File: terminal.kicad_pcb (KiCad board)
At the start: 2 copper layers, 135 x 75 mm, 41 parts, among them J1 L77HDE15SD1CH4F-ND, J2 Mini-DIN-6, J3 UART Connector, J4 DEBUG UART HEADER, J5 Power, Q1 BSS138, Q2 BSS138, SW1 CT2088-ND, U1 CYC1000, U2 MAX3232

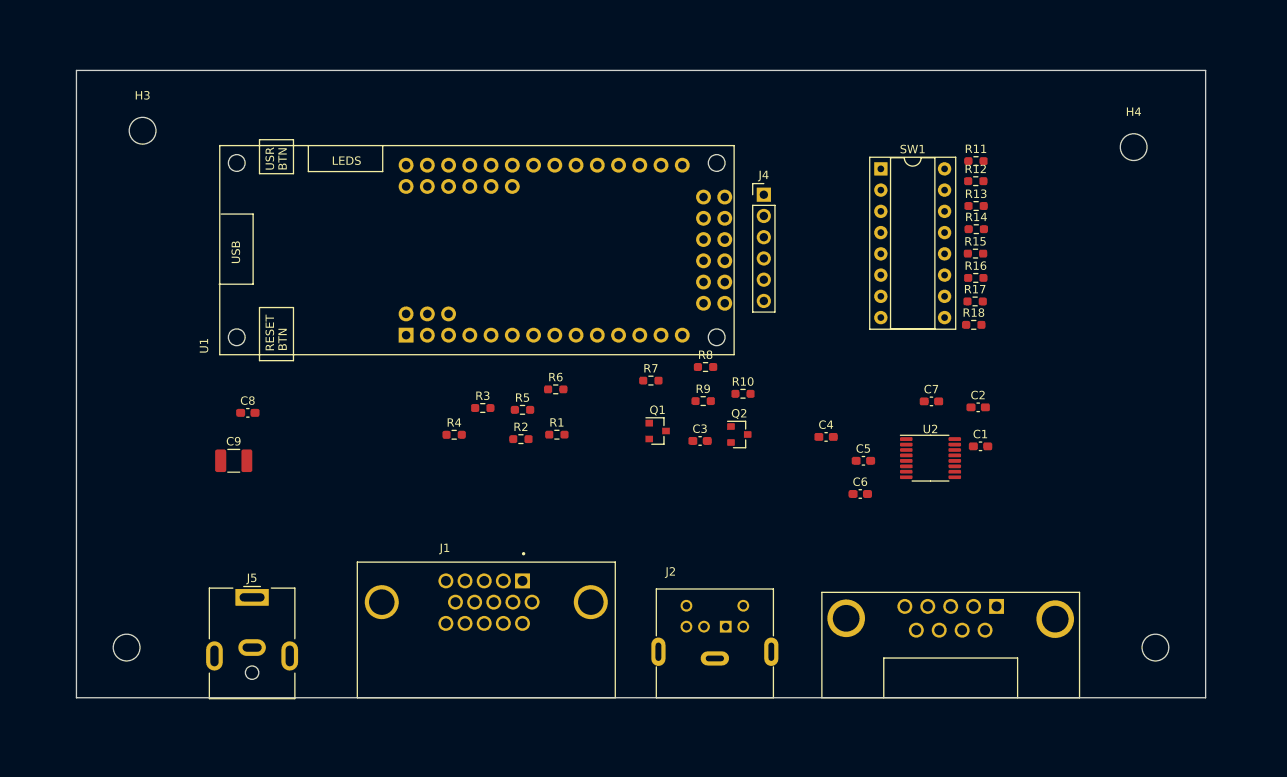
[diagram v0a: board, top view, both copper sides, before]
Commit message: Wiring connectors
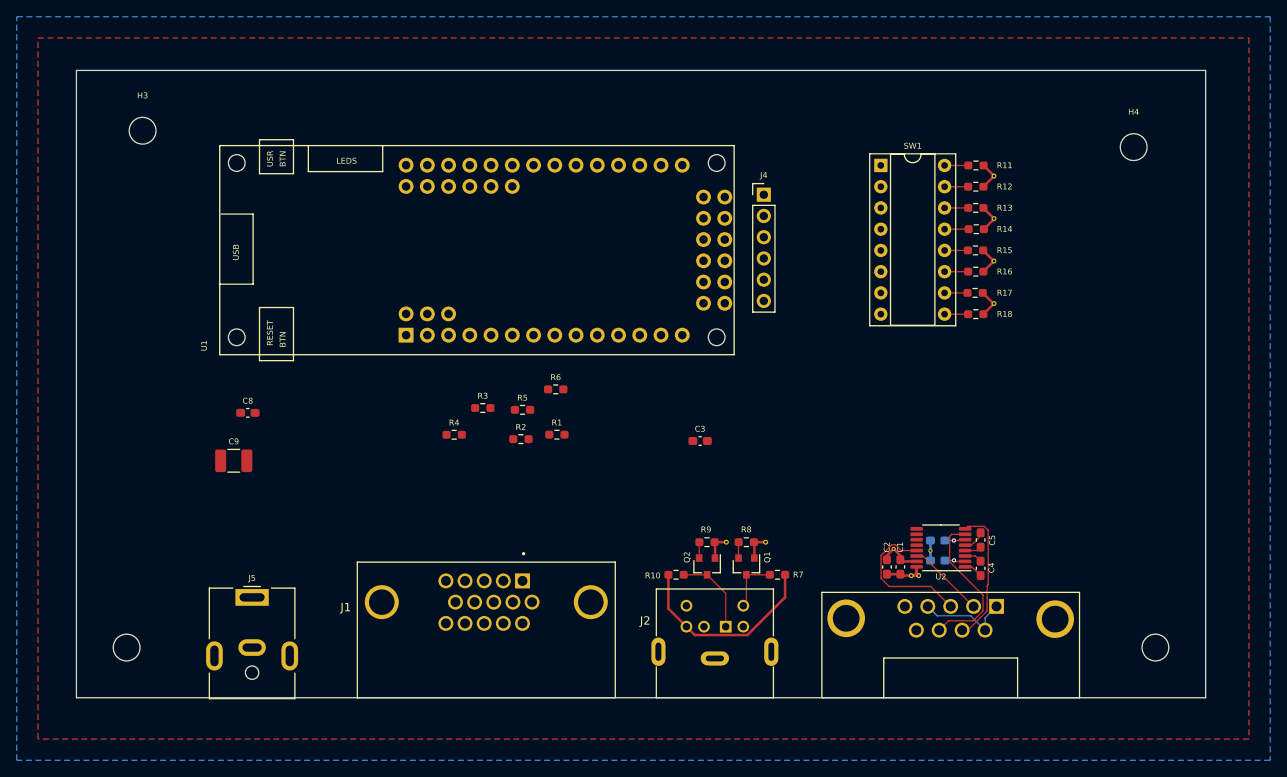
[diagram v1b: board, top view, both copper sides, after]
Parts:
- added REF**: VIA-0.6mm, falco_VIAS:VIA-0.6mm, F.Cu at (112.4, 131.4)
- added REF**: VIA-0.6mm, falco_VIAS:VIA-0.6mm, F.Cu at (139.7, 87.6)
- added REF**: VIA-0.6mm, falco_VIAS:VIA-0.6mm, F.Cu at (107.7, 131.4)
- added REF**: VIA-0.6mm, falco_VIAS:VIA-0.6mm, F.Cu at (127.7, 132.2)
- added REF**: VIA-0.6mm, falco_VIAS:VIA-0.6mm, F.Cu at (130.7, 135.4)
- added REF**: VIA-0.6mm, falco_VIAS:VIA-0.6mm, F.Cu at (132.1, 132.4)
- added REF**: VIA-0.6mm, falco_VIAS:VIA-0.6mm, F.Cu at (129.8, 135.4)
- added REF**: VIA-0.6mm, falco_VIAS:VIA-0.6mm, F.Cu at (139.7, 97.8)
- added REF**: VIA-0.6mm, falco_VIAS:VIA-0.6mm, F.Cu at (139.7, 102.9)
- added REF**: VIA-0.6mm, falco_VIAS:VIA-0.6mm, F.Cu at (139.7, 92.7)
- C6, C7: moved to B.Cu
- moved R7 27.7 mm to (113.8, 135.3), turned to 180 degrees
- moved C4 24.3 mm to (138.1, 134.5), turned to 90 degrees
- moved R10 23.1 mm to (101.7, 135.3)
- moved C2 22.0 mm to (126.9, 134.4), turned to 90 degrees
- moved R8 21.5 mm to (110.1, 131.4), turned to 180 degrees
- moved Q1 19.4 mm to (110.1, 134.3), turned to 270 degrees
- moved C7 19.0 mm to (133.0, 133.6), turned to 180 degrees
- moved C1 17.3 mm to (128.5, 134.4), turned to 90 degrees
- moved C5 16.9 mm to (138.1, 131.1), turned to 90 degrees
- moved R9 16.9 mm to (105.4, 131.4), turned to 180 degrees
- moved Q2 16.2 mm to (105.4, 134.3), turned to 270 degrees
- moved U2 10.8 mm to (133.3, 132.1), turned to 180 degrees
- moved C6 10.8 mm to (133.0, 131.2), turned to 180 degrees
- moved R18 1.30 mm to (137.5, 104.1), turned to 180 degrees
- moved R17 1.02 mm to (137.4, 101.6), turned to 180 degrees
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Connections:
- J2 pad S1: (no net) -> GND
- J2 pad S2: (no net) -> GND
- J2 pad S3: (no net) -> GND
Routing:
- net +3V3: track 0.00 -> 27.6 mm
- net +5V: track 0.00 -> 23.9 mm
- net /CTS: track 0.00 -> 18.7 mm
- net /TXD: track 0.00 -> 17.5 mm
- net /RTS: track 0.00 -> 16.7 mm
- net Net-(J3-Pad1): track 0.00 -> 11.4 mm
- net Net-(J2-Pad1): track 0.00 -> 9.92 mm
- net /RXD: track 0.00 -> 9.31 mm
- net GND: track 0.00 -> 7.70 mm
- net Net-(J2-Pad5): track 0.00 -> 6.65 mm
- net /DIP_SW3: track 0.00 -> 2.88 mm
- net /DIP_SW0: track 0.00 -> 2.84 mm
- net /DIP_SW1: track 0.00 -> 2.82 mm
- net /DIP_SW7: track 0.00 -> 2.81 mm
- net /DIP_SW5: track 0.00 -> 2.81 mm
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- added copper zone on B.Cu, net +3V3
- added copper zone on F.Cu, net GND
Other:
- net class Default: clearance 0.2 -> 0.1524; trace_width 0.25 -> 0.1524; via_dia 0.8 -> 0.508; via_drill 0.4 -> 0.254
- net class Power added: clearance 0.1524, trace_width 0.3048, via_dia 0.508, via_drill 0.254
- rule pad_to_mask_clearance: 0 -> 0.0508
- rule trace_clearance: 0.2 -> 0.1524
- rule trace_min: 0.2 -> 0.1524
- rule via_min_drill: 0.3 -> 0.254
- rule via_min_size: 0.4 -> 0.508

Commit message: Should be pretty close
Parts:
- removed the REF** at (112.4, 131.4)
- removed the REF** at (139.7, 87.6)
- removed the REF** at (107.7, 131.4)
- removed the REF** at (130.7, 135.4)
- removed the REF** at (132.1, 132.4)
- removed the REF** at (129.8, 135.4)
- removed the REF** at (139.7, 97.8)
- removed the REF** at (139.7, 102.9)
- removed the REF** at (139.7, 92.7)
- added C10: 0.1u, Capacitor_SMD:C_0603_1608Metric_Pad1.08x0.95mm_HandSolder, F.Cu at (109.5, 127.8)
- added REF**: VIA-0.6mm, falco_VIAS:VIA-0.6mm, F.Cu at (111.4, 126.8)
- added REF**: VIA-0.6mm, falco_VIAS:VIA-0.6mm, F.Cu at (107.5, 126.8)
- added REF**: VIA-0.6mm, falco_VIAS:VIA-0.6mm, F.Cu at (110.4, 121.7)
- added REF**: VIA-0.6mm, falco_VIAS:VIA-0.6mm, F.Cu at (108.0, 121.7)
- added REF**: VIA-0.6mm, falco_VIAS:VIA-0.6mm, B.Cu at (135.2, 136.0)
- C1, C2, C3, C4, C5, Q1, Q2, R1, R10, R11, R12, R13, R14, R15, R16, R17, R18, R2, R3, R4, R5, R6, R7, R8, R9, REF**, U2: moved to B.Cu
- C6, C7: moved to F.Cu
- moved H3 21.9 mm to (36.0, 104.0)
- moved C3 20.2 mm to (100.5, 139.1), turned to 270 degrees
- moved H4 20.0 mm to (159.0, 104.0)
- moved C8 19.5 mm to (48.7, 135.4), turned to 180 degrees
- moved R6 19.2 mm to (78.0, 129.9), turned to 90 degrees
- moved J4 17.3 mm to (114.7, 107.0)
- moved R17 17.1 mm to (140.5, 118.4)
- moved R15 17.1 mm to (140.4, 113.3)
- moved U1 17.0 mm to (72.3, 123.5)
- moved SW1 17.0 mm to (129.1, 103.2)
- moved R13 17.0 mm to (140.4, 108.2)
- moved R16 17.0 mm to (140.4, 115.9)
- moved R18 17.0 mm to (140.4, 120.9)
- moved R12 17.0 mm to (140.4, 105.7)
- moved R11 17.0 mm to (140.4, 103.2)
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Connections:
- U1 pad 2: /PIXEL_R1 -> /PIXEL_B1
- U1 pad 3: /PIXEL_R2 -> /PIXEL_B2
- U1 pad 6: /PIXEL_B1 -> /PIXEL_R1
- U1 pad 7: /PIXEL_B2 -> /PIXEL_R2
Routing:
- net /UART_RTS: track 0.00 -> 69.1 mm
- net /UART_CTS: track 0.00 -> 66.0 mm
- net /DIP_SW6: track 2.74 -> 55.8 mm
- net /VCC-5.0: track 0.00 -> 52.3 mm
- net /DIP_SW5: track 2.81 -> 52.1 mm
- net +5V: track 23.9 -> 72.5 mm
- net /UART_RX: track 0.00 -> 46.3 mm
- net /DIP_SW4: track 2.78 -> 48.6 mm
- net /UART_TX: track 0.00 -> 42.5 mm
- net /DIP_SW3: track 2.88 -> 44.9 mm
- net /DIP_SW2: track 2.81 -> 41.3 mm
- net /DIP_SW1: track 2.82 -> 37.7 mm
- net /DIP_SW7: track 2.81 -> 36.0 mm
- net /DIP_SW0: track 2.84 -> 35.4 mm
- net /VSYNC: track 0.00 -> 30.3 mm
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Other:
- board size 135 x 75 mm -> 135 x 52 mm
- board text added: "Terminal v1.0 (C) 2021 Falco Engineering"

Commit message: V1 looks good
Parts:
- added R19: 100, Resistor_SMD:R_0603_1608Metric_Pad0.98x0.95mm_HandSolder, B.Cu at (89.9, 129.1)
- added R20: 100, Resistor_SMD:R_0603_1608Metric_Pad0.98x0.95mm_HandSolder, B.Cu at (91.7, 129.1)
- H1, H2, H3, H4: value MountingHole -> MountingHole_Pad; footprint MountingHole:MountingHole_3.2mm_M3 -> MountingHole:MountingHole_3.2mm_M3_DIN965_Pad
- moved J2 6.50 mm to (106.3, 150.0)
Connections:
- net Net-(C4-Pad1) renamed /C1+
- net Net-(C4-Pad2) renamed /C1-
- net Net-(C5-Pad1) renamed /C2+
- net Net-(C5-Pad2) renamed /C2-
- net Net-(C6-Pad1) renamed /VS-
- net Net-(C7-Pad1) renamed /VS+
- H1 pad 1: (no net) -> GND
- H2 pad 1: (no net) -> GND
- H3 pad 1: (no net) -> GND
- H4 pad 1: (no net) -> GND
- J1 pad 13: /HSYNC -> Net-(J1-Pad13)
- J1 pad 14: /VSYNC -> Net-(J1-Pad14)
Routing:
- net /VSYNC: track 30.3 -> 5.14 mm
- net Net-(J1-Pad14): track 0.00 -> 23.3 mm
- net /HSYNC: track 25.2 -> 4.82 mm
- net Net-(J1-Pad13): track 0.00 -> 18.6 mm

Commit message: Sense of RX/TX and CTS/RTS were backwards.
Fortunately, that is easy to fix in the FPGA by remapping the signals to
different pins.
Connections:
- U1 pad 10: /UART_RX -> /UART_TX
- U1 pad 11: /UART_TX -> /UART_RX
- U1 pad 29: /UART_RTS -> /UART_CTS
- U1 pad 30: /UART_CTS -> /UART_RTS
- U2 pad 10: /UART_CTS -> /UART_RTS
- U2 pad 11: /UART_RX -> /UART_TX
- U2 pad 12: /UART_TX -> /UART_RX
- U2 pad 9: /UART_RTS -> /UART_CTS
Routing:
- net /UART_TX: track 42.5 -> 46.3 mm
- net /UART_RX: track 46.3 -> 42.5 mm
- net /UART_RTS: track 69.1 -> 66.0 mm
- net /UART_CTS: track 66.0 -> 69.1 mm

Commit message: Convert to KiCad 6 series
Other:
- net class Default removed
- net class Power removed
